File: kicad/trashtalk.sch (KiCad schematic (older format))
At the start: 12 parts, among them U1 ARDUINO_PRO_MINI_5V, U2 DFPlayer_Mini, U3 LM386MODULE

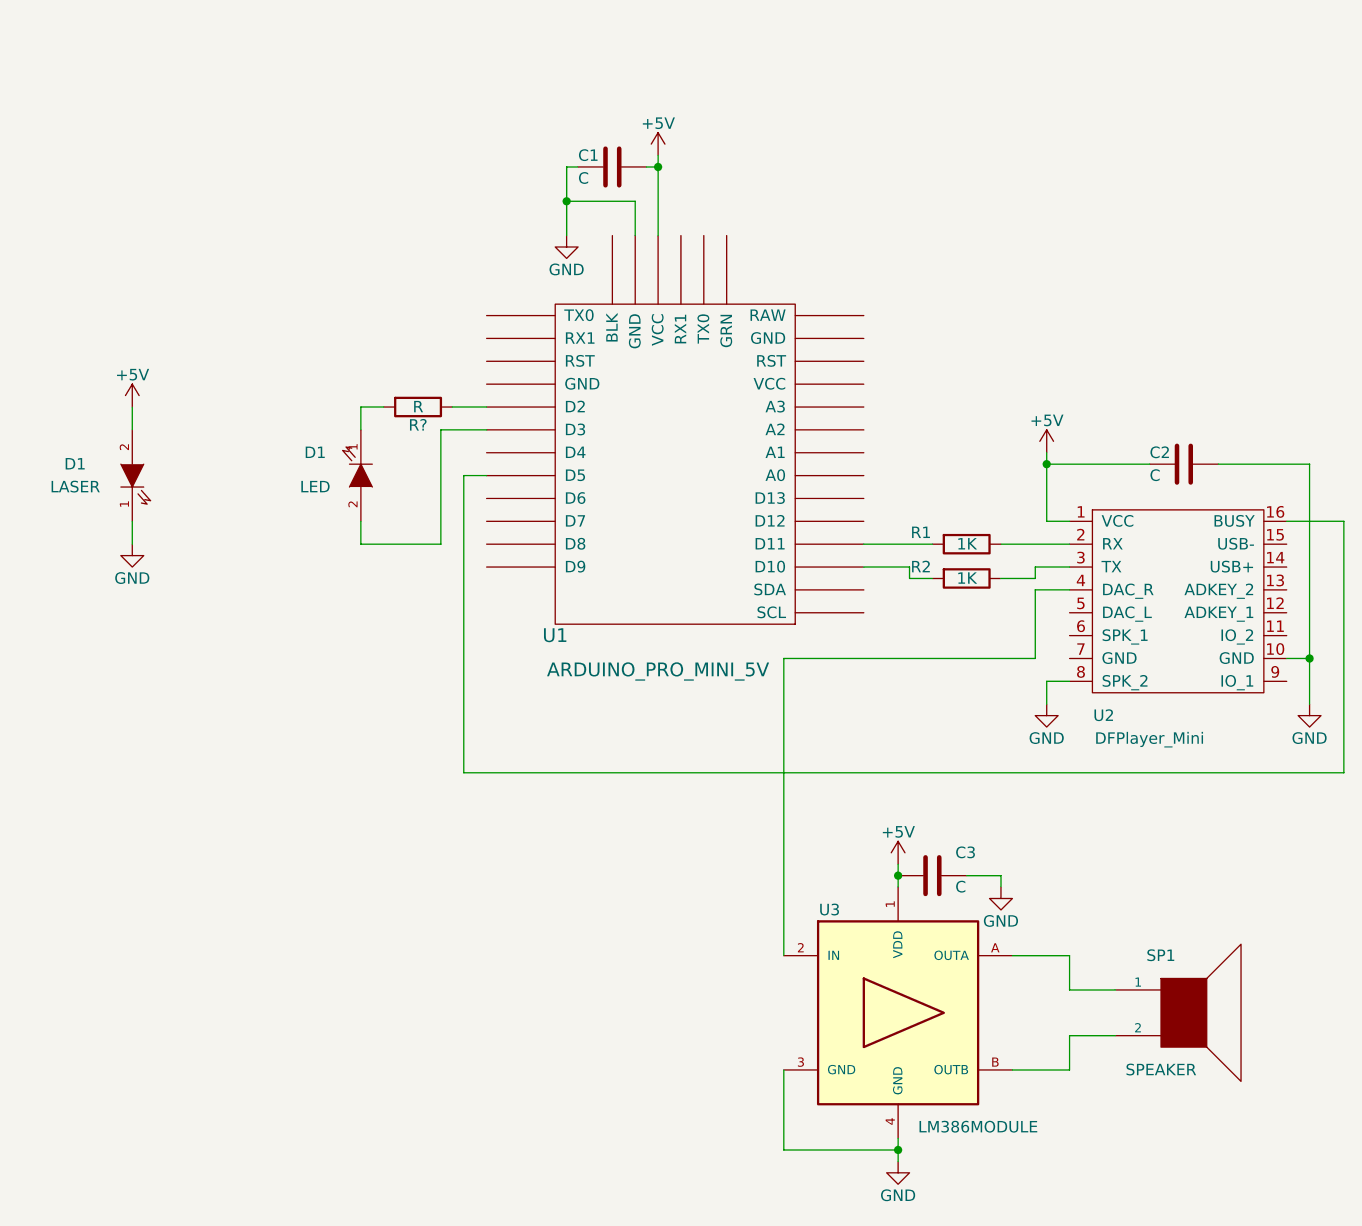
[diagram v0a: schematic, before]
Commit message: Update for veroboard layout.
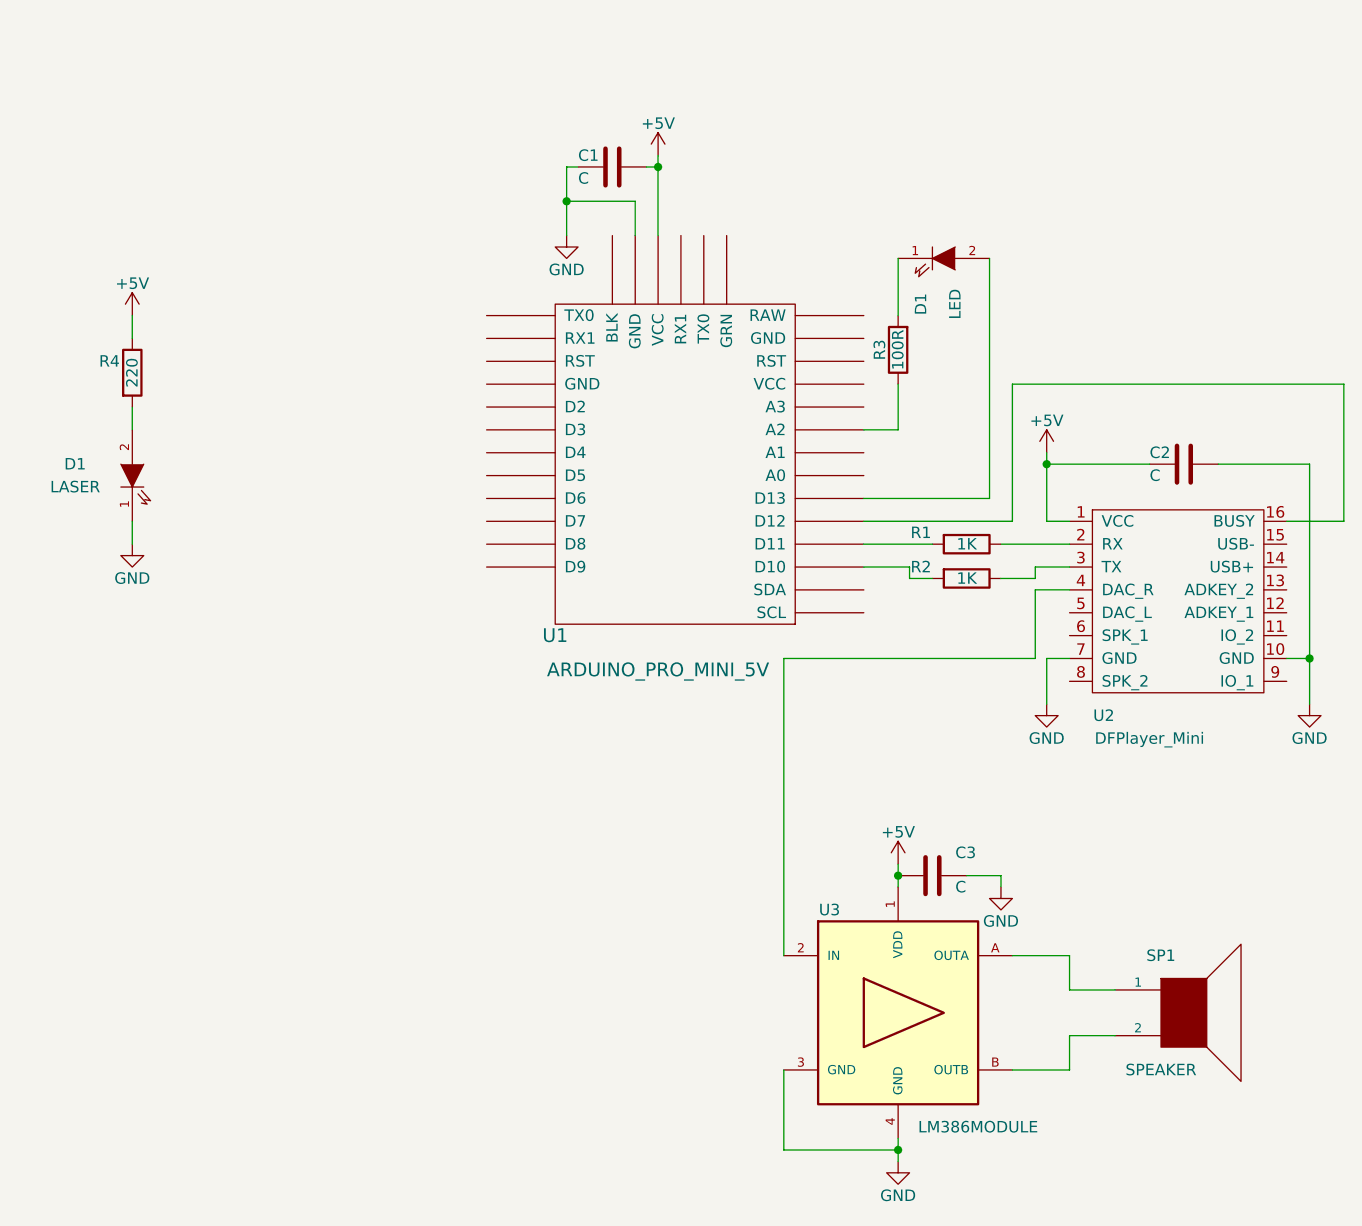
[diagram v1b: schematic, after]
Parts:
- added R4: 220, symbol R
- R3: renamed from R?; value R -> 100R
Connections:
- net +5V: now also R4.1; no longer D1.2 (A)
- net GND: now also U2.7 (GND); no longer U2.8 (SPK_2)
- new net: D1.2 (A), R4.2
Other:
- moved on the sheet: D1, R3
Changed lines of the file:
@@
 Connection ~ 5550 3500
 Wire Wire Line
-	5650 4450 5550 4450
-Wire Wire Line
-	5550 4450 5550 4550
+	5550 4350 5550 4550
 Wire Wire Line
 	6600 4350 6700 4350
 Wire Wire Line
 	6700 3500 6700 4550
-Wire Wire Line
-	3000 3550 3000 4850
-Wire Wire Line
-	3000 4850 6850 4850
-Wire Wire Line
-	6850 4850 6850 3750
 Wire Wire Line
 	6850 3750 6600 3750
@@
 Wire Wire Line
 	3850 2150 3850 2500
-Wire Wire Line
-	3000 3550 3100 3550
 $Comp
 L C C1
@@
 Connection ~ 4900 6500
 $Comp
-L R R?
+L R R3
 U 1 1 581FC62F
-P 2800 3250
-F 0 "R?" V 2880 3250 50  0000 C CNN
-F 1 "R" V 2800 3250 50  0000 C CNN
-F 2 "" V 2730 3250 50  0000 C CNN
-F 3 "" H 2800 3250 50  0000 C CNN
-	1    2800 3250
-	0    1    1    0
+P 4900 3000
+F 0 "R3" V 4980 3000 50  0000 C CNN
+F 1 "100R" V 4900 3000 50  0000 C CNN
+F 2 "" V 4830 3000 50  0000 C CNN
+F 3 "" H 4900 3000 50  0000 C CNN
+	1    4900 3000
+	-1   0    0    1
 $EndComp
 $Comp
 L LED D1
 U 1 1 581FC672
-P 2550 3550
-F 0 "D1" V 2450 3350 50  0000 C CNN
-F 1 "LED" V 2600 3350 50  0000 C CNN
-F 2 "" H 2550 3550 50  0000 C CNN
-F 3 "" H 2550 3550 50  0000 C CNN
-	1    2550 3550
-	0    1    1    0
-$EndComp
-Wire Wire Line
-	2650 3250 2550 3250
-Wire Wire Line
-	2550 3250 2550 3350
-Wire Wire Line
-	2950 3250 3100 3250
-Wire Wire Line
-	3100 3350 2900 3350
-Wire Wire Line
-	2900 3350 2900 3850
-Wire Wire Line
-	2900 3850 2550 3850
-Wire Wire Line
-	2550 3850 2550 3750
+P 5100 2600
+F 0 "D1" V 5000 2400 50  0000 C CNN
+F 1 "LED" V 5150 2400 50  0000 C CNN
+F 2 "" H 5100 2600 50  0000 C CNN
+F 3 "" H 5100 2600 50  0000 C CNN
+	1    5100 2600
+	1    0    0    -1
+$EndComp
 $Comp
 L LED D1
@@
 L +5V #PWR?
 U 1 1 581FC990
-P 1550 3250
-F 0 "#PWR?" H 1550 3100 50  0001 C CNN
-F 1 "+5V" H 1550 3390 50  0000 C CNN
-F 2 "" H 1550 3250 50  0000 C CNN
-F 3 "" H 1550 3250 50  0000 C CNN
-	1    1550 3250
+P 1550 2850
+F 0 "#PWR?" H 1550 2700 50  0001 C CNN
+F 1 "+5V" H 1550 2990 50  0000 C CNN
+F 2 "" H 1550 2850 50  0000 C CNN
+F 3 "" H 1550 2850 50  0000 C CNN
+	1    1550 2850
 	1    0    0    -1
 $EndComp
@@
 Wire Wire Line
 	1550 3350 1550 3250
+Wire Wire Line
+	5550 4350 5650 4350
+Wire Wire Line
+	4750 3750 5400 3750
+Wire Wire Line
+	4750 3350 4900 3350
+Wire Wire Line
+	5400 3750 5400 3150
+Wire Wire Line
+	5400 3150 6850 3150
+Wire Wire Line
+	6850 3150 6850 3750
+Wire Wire Line
+	4900 2600 4900 2850
+Wire Wire Line
+	4900 3350 4900 3150
+Wire Wire Line
+	5300 2600 5300 3650
+Wire Wire Line
+	5300 3650 4750 3650
+$Comp
+L R R4
+U 1 1 58334706
+P 1550 3100
+F 0 "R4" H 1450 3150 50  0000 C CNN
+F 1 "220" V 1550 3100 50  0000 C CNN
+F 2 "" V 1480 3100 50  0000 C CNN
+F 3 "" H 1550 3100 50  0000 C CNN
+	1    1550 3100
+	1    0    0    -1
+$EndComp
+Wire Wire Line
+	1550 2850 1550 2950
 $EndSCHEMATC

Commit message: Add connectors.
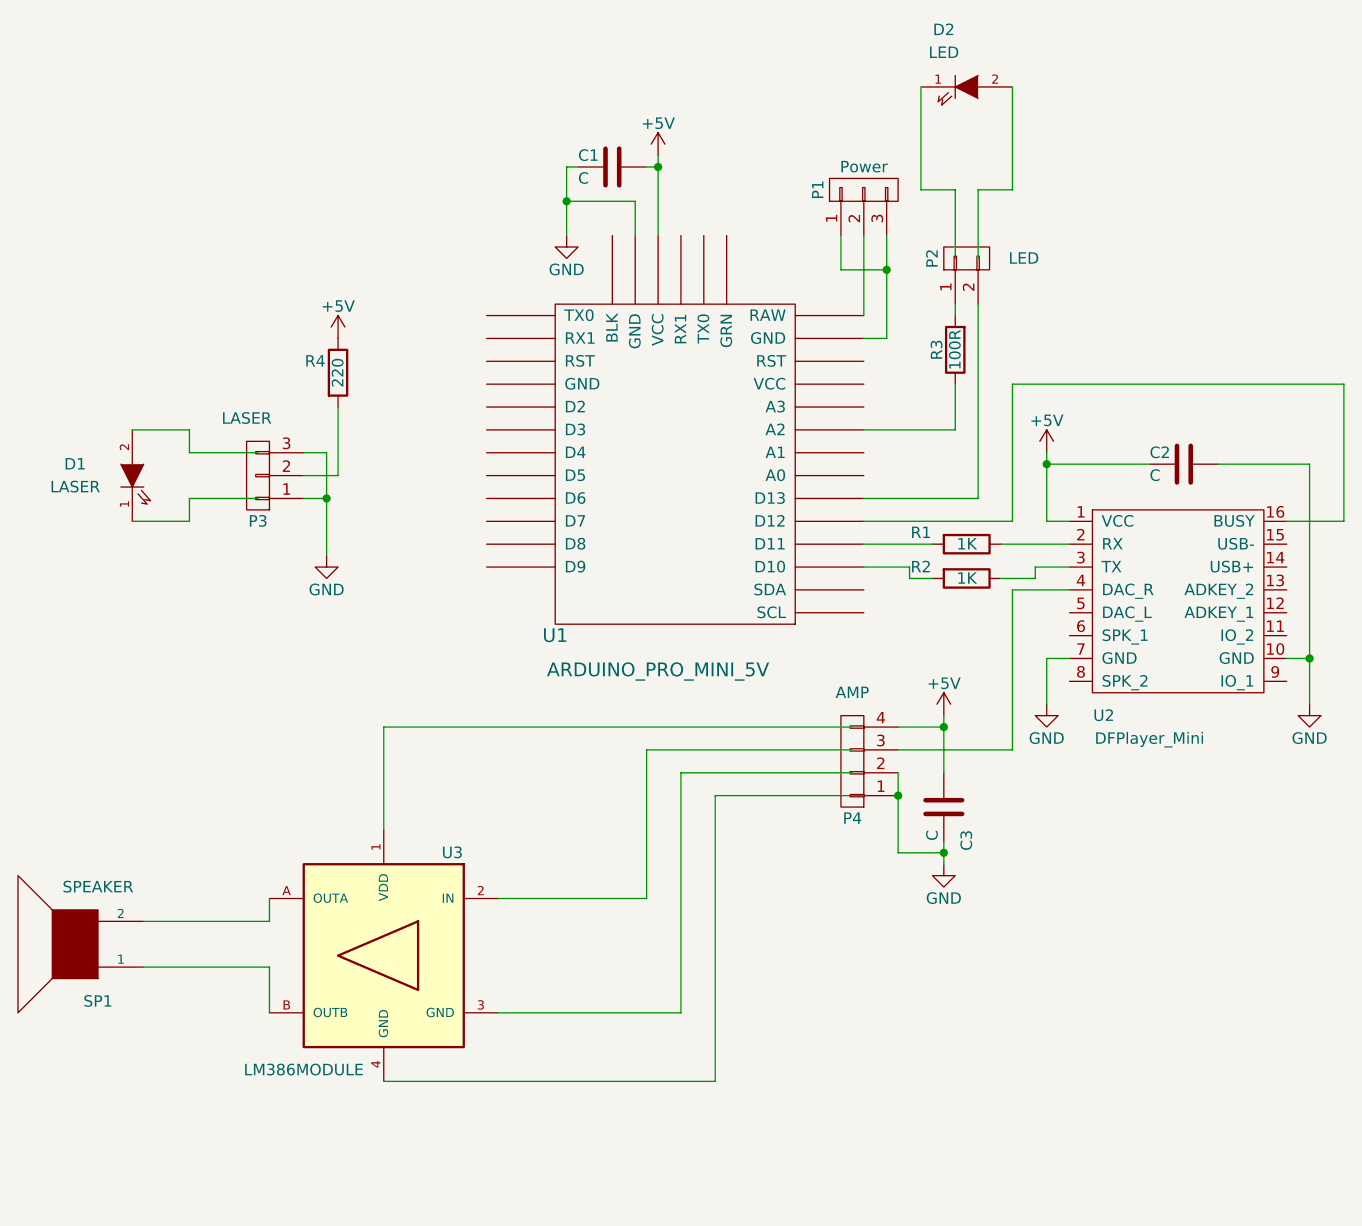
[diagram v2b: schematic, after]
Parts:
- added P1: Power, symbol CONN_01X03
- added P2: LED, symbol CONN_01X02
- added P3: LASER, symbol CONN_01X03
- added P4: AMP, symbol CONN_01X04
- renumbered D1 to D2
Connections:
- wire segments 51 -> 77
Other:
- moved on the sheet: C3, D2, R3, R4, SP1, U3
